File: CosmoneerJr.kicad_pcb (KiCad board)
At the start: 4 copper layers, 70 x 50 mm, 83 parts, among them J1 Header, J13 Header, J17 Header, J18 Header, J5 Header, J9 Header, P1 .1" Header, P2 Header, P3 SM04B-SRSS-TB, P4 Header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

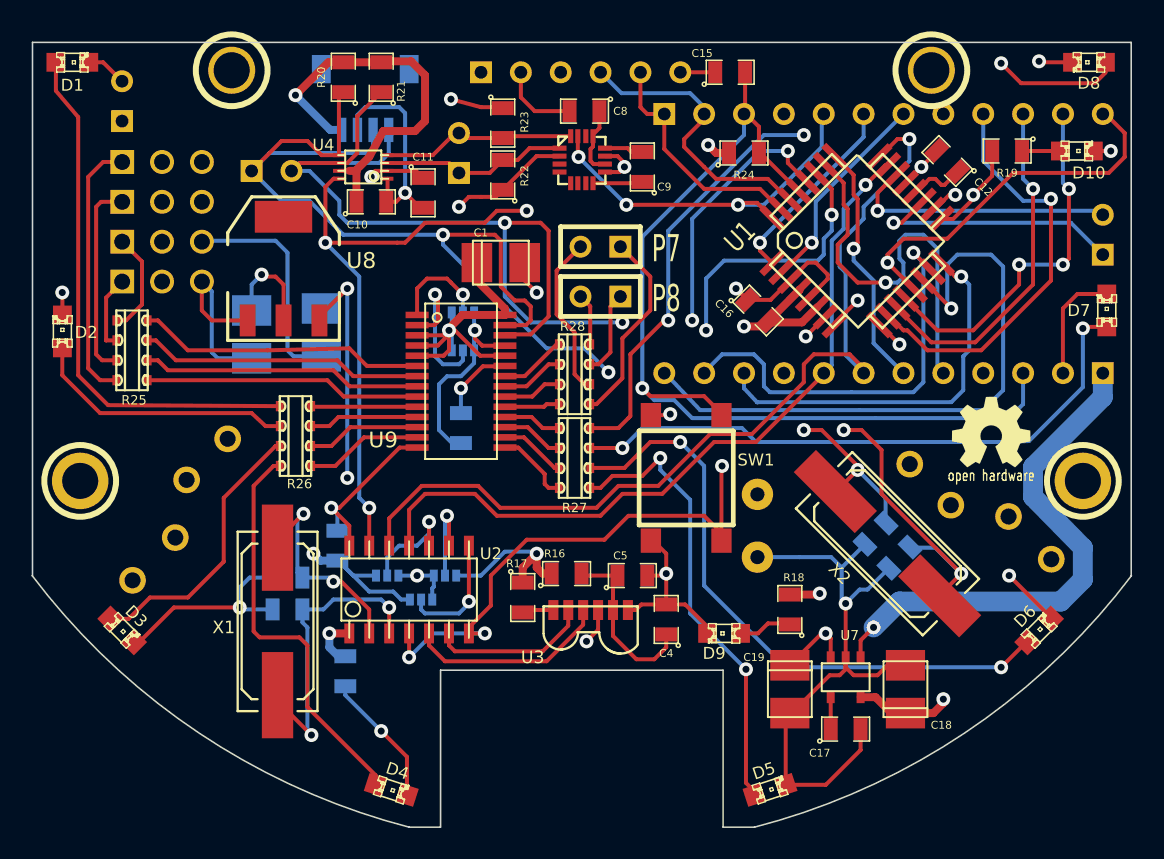
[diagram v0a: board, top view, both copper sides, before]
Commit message: Rev Zero Cleanup
Eliminated vias and extra verticies in traces.  Prepared bottom
silkscreen to merge with bottom layer.
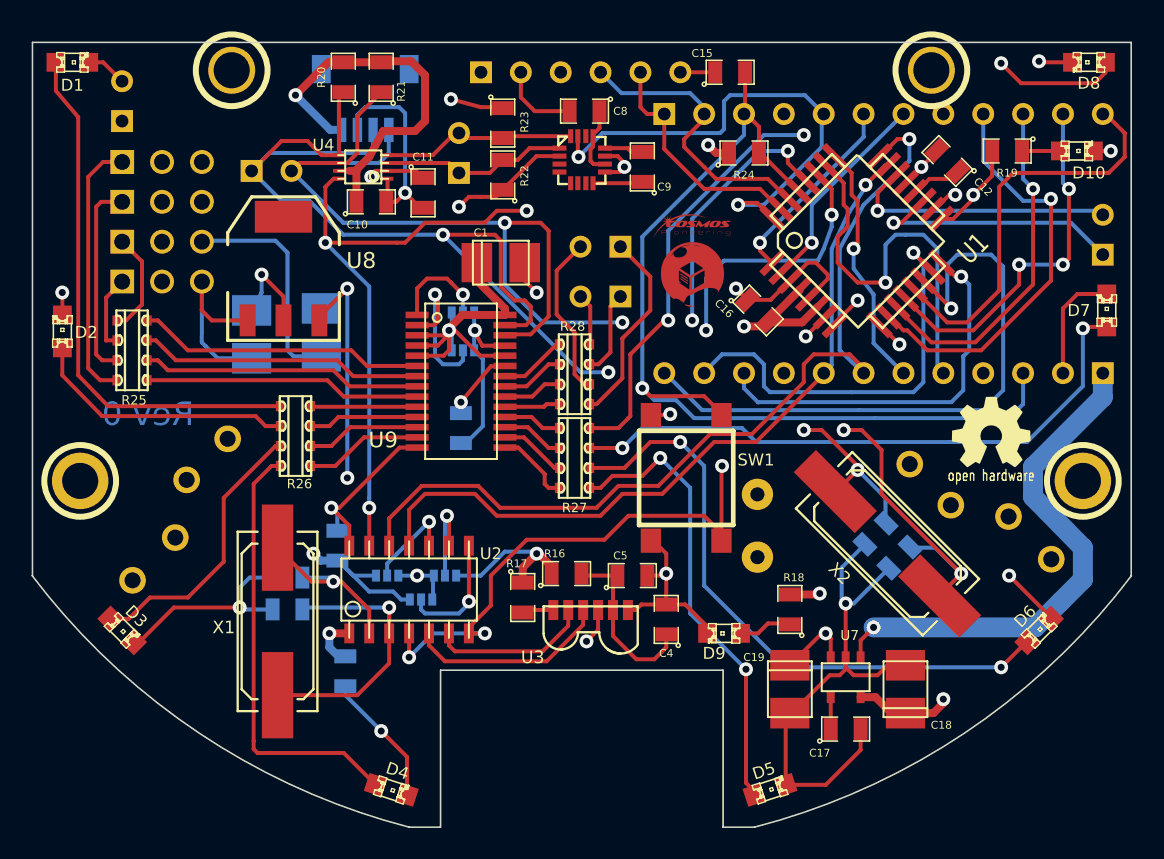
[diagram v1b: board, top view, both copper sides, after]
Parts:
- added VAL: REF, LOGO, F.Cu at (232.0, 129.7)
- P7, P8: moved to B.Cu
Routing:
- net /INT: track 24.5 -> 31.8 mm, vias 3 -> 2
- net GND: track 206.3 -> 199.2 mm
- net N-0000061: track 13.8 -> 11.1 mm, vias 2 -> 1
- net /D9: track 24.1 -> 25.9 mm, vias 1 -> 0
- net N-0000036: track 25.9 -> 27.7 mm
- net /I2C_SCL_5V: track 79.6 -> 78.6 mm
- net N-0000010: track 6.73 -> 6.06 mm
- net N-0000062: track 19.3 -> 18.7 mm, vias 2 -> 1
- net /I2C_SDA_5V: track 85.4 -> 84.8 mm
- net +3.3V: track 49.4 -> 48.8 mm
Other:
- rule pad_to_mask_clearance: 0 -> 0.152
- board text added: "Rev 0"

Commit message: Rev ZeroOne Prototype
Parts added, Schematic updated and PCB updated and Mfg files generated
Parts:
- removed C10, C11: 0.1uf, SM0805
- removed C8: 4.7uf, SM0805
- removed C9: 0.22uf, SM0805
- removed P5: Header, SIL-2
- removed R22, R23: 10K, SM0805
- removed U4: PCA9306, pca9306dcu
- removed U5: HMC5883, HMC5883L_bigpads
- added D11: 1N4001, DO-214AC(SMA), F.Cu at (197.4, 118.2)
- added F1: FUSE, SM1812, F.Cu at (206.0, 122.2)
- added GY-271: U10, GY-271, F.Cu at (221.1, 125.3)
- C13, C14: value 22pf -> 15pf; moved to F.Cu
- C2, C20, C21, C3, R7: moved to F.Cu
- C6, C7: value 22pf -> 27pf; moved to F.Cu
- R25, R28: value 220 Ohm -> 330 Ohm; footprint r_CN2A4 -> r_cat16-4
- R26, R27: footprint r_CN2A4 -> r_cat16-4
- SW1: footprint SW_PUSH_SMD -> smd_push2
- moved P7 29.6 mm to (197.0, 133.0)
- moved P8 29.5 mm to (197.0, 135.5)
- moved G*** 23.6 mm to (228.0, 144.8)
- moved R28 23.2 mm to (201.3, 136.1)
- moved SW1 14.0 mm to (244.1, 149.1), turned to 180 degrees
- moved C14 11.2 mm to (232.8, 144.0), turned to 0 degrees
- moved X2 10.1 mm to (237.0, 140.2), turned to 0 degrees
- moved C7 9.93 mm to (209.0, 158.6), turned to 0 degrees
- moved C20 9.53 mm to (210.9, 127.1), turned to 0 degrees
- moved C3 8.92 mm to (212.5, 155.4), turned to 270 degrees
- moved C1 8.28 mm to (224.7, 135.8)
- moved R7 7.31 mm to (224.5, 138.6), turned to 180 degrees
- moved C21 7.28 mm to (204.9, 127.1), turned to 180 degrees
- moved C6 6.71 mm to (209.0, 145.0), turned to 0 degrees
- moved P4 6.11 mm to (211.3, 123.6)
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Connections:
- 1PIN pad 1: (no net) -> GND
- C20 pad 1: +3.3V -> +5V
- D1 pad 1: N-0000033 -> N-0000037
- D2 pad 1: N-0000034 -> N-0000038
- D3 pad 1: N-0000035 -> N-0000039
- D4 pad 1: N-0000036 -> N-0000040
- D5 pad 1: N-0000037 -> N-0000041
- D6 pad 1: N-0000038 -> N-0000036
- D7 pad 1: N-0000039 -> N-0000042
- D8 pad 1: N-0000040 -> N-0000043
- J1 pad 1: N-0000059 -> N-0000033
- J13 pad 1: N-0000058 -> N-0000032
- J18 pad 1: VCC -> /RAW
- J5 pad 1: N-0000056 -> N-0000034
- J9 pad 1: N-0000057 -> N-0000035
- JP4 pad 2: /RA0 -> /RA1
- JP5 pad 2: /RA1 -> /RA2
- P3 pad FIT@: (no net) -> GND
- P6 pad 1: VCC -> /RAW
- P7 pad 1: N-0000042 -> N-0000027
- P7 pad 2: N-0000043 -> N-0000028
- P8 pad 1: N-0000041 -> N-0000022
- P8 pad 2: N-0000044 (its old number) -> N-0000023
- R25 pad 1: /SERVO1_PWM -> N-0000033
- R25 pad 2: N-0000059 -> N-0000034
- R25 pad 3: /MOTOR1_PWM -> N-0000035
- R25 pad 4: N-0000056 -> N-0000032
- R25 pad 5: /SERVO2_PWM -> /MOTOR2_PWM
- R25 pad 6: N-0000057 -> /SERVO2_PWM
- R25 pad 7: /MOTOR2_PWM -> /MOTOR1_PWM
- R25 pad 8: N-0000058 -> /SERVO1_PWM
- R26 pad 1: /PWMSPARE1 -> N-0000037
- R26 pad 2: N-0000033 -> N-0000038
- R26 pad 3: /PWMSPARE2 -> N-0000039
- R26 pad 4: N-0000034 -> N-0000040
- R26 pad 5: /PWMSPARE3 -> /PWMSPARE4
- R26 pad 6: N-0000035 -> /PWMSPARE3
- R26 pad 7: /PWMSPARE4 -> /PWMSPARE2
- R26 pad 8: N-0000036 -> /PWMSPARE1
- R27 pad 1: /PWMSPARE5 -> N-0000041
- R27 pad 2: N-0000037 -> N-0000036
- R27 pad 3: /PWMSPARE6 -> N-0000042
- R27 pad 4: N-0000038 -> N-0000043
- R27 pad 5: /PWMSPARE7 -> /PWMSPARE8
- R27 pad 6: N-0000039 -> /PWMSPARE7
- R27 pad 7: /PWMSPARE8 -> /PWMSPARE6
- R27 pad 8: N-0000040 -> /PWMSPARE5
- R28 pad 1: /SERVO3_PWM -> N-0000027
- R28 pad 2: N-0000042 -> N-0000028
- R28 pad 3: /MOTOR3_PWM -> N-0000022
- R28 pad 4: N-0000043 -> N-0000023
- R28 pad 5: /SERVO4_PWM -> /MOTOR4_PWM
- R28 pad 6: N-0000041 -> /SERVO4_PWM
- R28 pad 7: /MOTOR4_PWM -> /MOTOR3_PWM
- R28 pad 8: N-0000044 (its old number) -> /SERVO3_PWM
- U8 pad 2: +3.3V -> +5V
- U8 pad 4: (no net) -> +5V
- U9 pad 1: /RA0 -> GND
- U9 pad 3: +5V -> /RA2
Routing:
- net /RAW: track 0.00 -> 131.3 mm
- net +3.3V: track 48.8 -> 0.00 mm, vias 4 -> 0
- net N-0000043: track 10.5 -> 50.5 mm, vias 0 -> 3
- net GND: track 199.2 -> 238.1 mm, vias 18 -> 24
- net VCC: track 146.2 -> 116.3 mm, vias 4 -> 2
- net ENABLE: track 94.2 -> 64.4 mm, vias 4 -> 3
- net N-0000042: track 12.6 -> 39.1 mm, vias 0 -> 2
- net N-0000041: track 5.42 -> 30.3 mm, vias 0 -> 2
- net N-0000033: track 34.1 -> 9.59 mm, vias 0 -> 1
- net /A0: track 48.2 -> 70.6 mm
- net /SERVO3_PWM: track 3.50 -> 25.6 mm, vias 0 -> 2
- net N-0000040: track 51.9 -> 30.2 mm, vias 3 -> 0
- net /I2C_SDA_5V: track 84.8 -> 63.9 mm, vias 4 -> 1
- net N-0000032: track 0.00 -> 20.9 mm
- net N-0000039: track 39.0 -> 18.6 mm, vias 2 -> 0
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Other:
- net class 5V: trace_width 0.508 -> 0.4
- board text added: "Rev 01"
- board text removed: "Rev 0"

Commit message: Rev 02
Fixes made to PCB for Rev 02.  Additional files for Rev 01/02 design
added to repository.
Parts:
- moved C15 6.23 mm to (232.7, 122.9), turned to 270 degrees
- moved R24 0.88 mm to (235.1, 122.9), turned to 270 degrees
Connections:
- SW1 pad 3: /RESET -> GND
- SW1 pad 4: GND -> /RESET
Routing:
- net /DTR: track 2.22 -> 7.79 mm
- net /RESET: track 88.2 -> 93.3 mm
- net /RXI: track 19.8 -> 23.1 mm
- net GND: track 238.1 -> 235.1 mm
- net /TXO: track 15.0 -> 17.4 mm
- net /I2C_SDA_5V: track 63.9 -> 66.0 mm
- net +5V: track 74.8 -> 76.7 mm
- net /I2C_SCL_5V: track 64.0 -> 62.8 mm
- net /INT: track 42.2 -> 41.5 mm
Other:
- board text added: "Rev 02"
- board text removed: "Rev 01"
